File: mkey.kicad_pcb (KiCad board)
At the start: 2 copper layers, 346.1 x 94.5 mm, 168 parts, among them J1 USB_C_REP_2.0, J2 24 pin LCD FPC connector, U1 ESP32-S3-WROOM-1, U2 SY8088

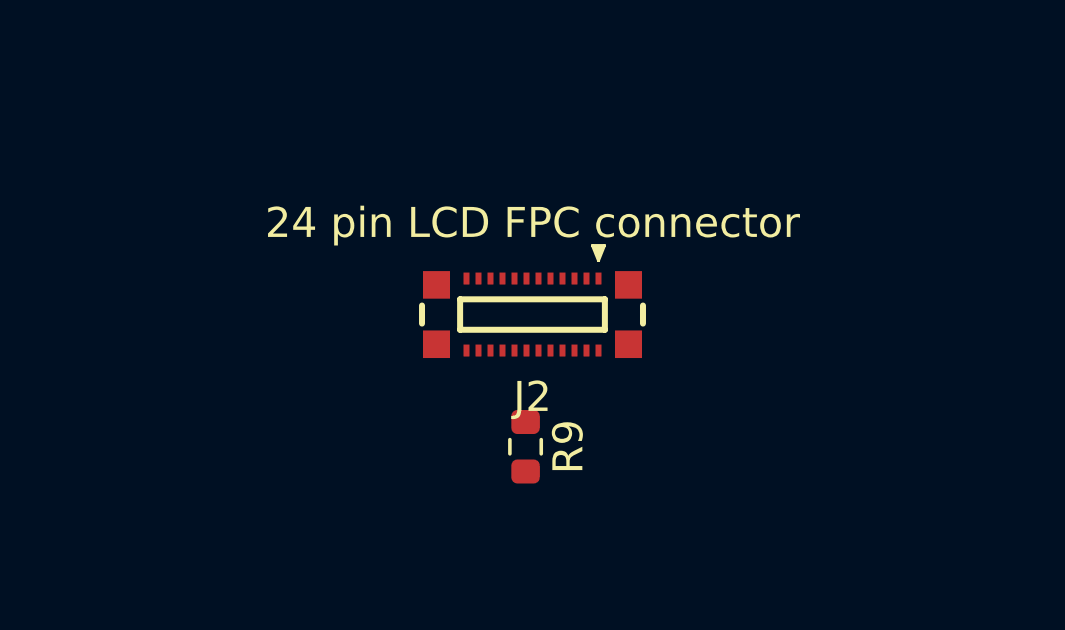
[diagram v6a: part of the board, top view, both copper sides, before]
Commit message: edit connector symbol to layout pins linearly, update pcb
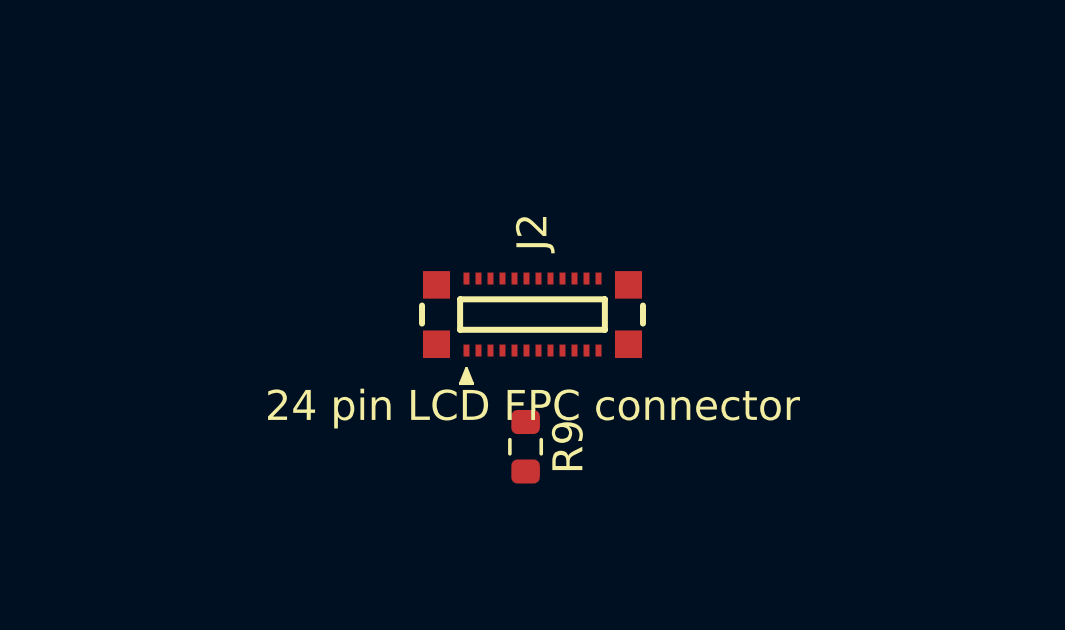
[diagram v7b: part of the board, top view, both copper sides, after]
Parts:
- J2: footprint CONN-SMD_24P-P0.40__X0400FVS-24-LPSN:CONN-SMD_24P-P0.40_X0400FVS-24-LPSN -> CONN-SMD_24P-P0.40_X0400FVS-24-LPSN-LINEAR:CONN-SMD_24P-P0.40_X0400FVS-24-LPSN-LINEAR
- turned J2 to 0 degrees
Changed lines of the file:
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@@
     )
   )
-  (footprint "CONN-SMD_24P-P0.40__X0400FVS-24-LPSN:CONN-SMD_24P-P0.40_X0400FVS-24-LPSN" (layer "F.Cu")
-    (at 358.18122 80.55628 180)
+  (footprint "CONN-SMD_24P-P0.40_X0400FVS-24-LPSN-LINEAR:CONN-SMD_24P-P0.40_X0400FVS-24-LPSN-LINEAR" (layer "F.Cu")
+    (at 358.18122 80.55628)
     (property "Sheetfile" "mkey.kicad_sch")
     (property "Sheetname" "")
     (property "ki_description" "Generic connector, single row, 01x24, script generated")
     (property "ki_keywords" "connector")
-    (fp_text reference "J2" (at 0 -2.75) (layer "F.SilkS")
+    (fp_text reference "J2" (at 0 -2.75 90) (layer "F.SilkS")
         (effects (font (size 1 1) (thickness 0.15)))
     )
@@
         (effects (font (size 1 1) (thickness 0.15)))
     )
-    (fp_text user "${REFERENCE}" (at -2.85557 0.29322 180 unlocked) (layer "Eco2.User")
+    (fp_text user "${REFERENCE}" (at -2.85557 0.29322 unlocked) (layer "Eco2.User")
         (effects (font (size 0.762 0.762) (thickness 0.254)) (justify left bottom))
     )
@@
     (fp_line (start 4 2) (end 4 -2)
       (stroke (width 0.1) (type solid)) (layer "Eco2.User"))
-    (pad "1" smd rect (at -2.20002 1.20002 180) (size 0.2 0.4) (layers "F.Cu" "F.Paste" "F.Mask")
+    (pad "1" smd rect (at 2.19997 -1.2) (size 0.2 0.4) (layers "F.Cu" "F.Paste" "F.Mask")
       (net 118 "LCD_RESET") (pinfunction "Pin_1") (pintype "passive") (thermal_bridge_angle 45))
-    (pad "2" smd rect (at -2.20002 -1.19997 180) (size 0.2 0.4) (layers "F.Cu" "F.Paste" "F.Mask")
+    (pad "2" smd rect (at 1.79997 -1.19997) (size 0.2 0.4) (layers "F.Cu" "F.Paste" "F.Mask")
       (net 7 "GND") (pinfunction "Pin_2") (pintype "passive") (thermal_bridge_angle 45))
-    (pad "3" smd rect (at -1.80002 1.20002 180) (size 0.2 0.4) (layers "F.Cu" "F.Paste" "F.Mask")
+    (pad "3" smd rect (at 1.39997 -1.19997) (size 0.2 0.4) (layers "F.Cu" "F.Paste" "F.Mask")
       (net 119 "TEAR EFFECT") (pinfunction "Pin_3") (pintype "passive") (thermal_bridge_angle 45))
-    (pad "4" smd rect (at -1.80002 -1.19997 180) (size 0.2 0.4) (layers "F.Cu" "F.Paste" "F.Mask")
+    (pad "4" smd rect (at 0.99997 -1.19997) (size 0.2 0.4) (layers "F.Cu" "F.Paste" "F.Mask")
       (net 7 "GND") (pinfunction "Pin_4") (pintype "passive") (thermal_bridge_angle 45))
-    (pad "5" smd rect (at -1.40002 1.20002 180) (size 0.2 0.4) (layers "F.Cu" "F.Paste" "F.Mask")
+    (pad "5" smd rect (at 0.59997 -1.19997) (size 0.2 0.4) (layers "F.Cu" "F.Paste" "F.Mask")
       (net 120 "LCD_CLK") (pinfunction "Pin_5") (pintype "passive") (thermal_bridge_angle 45))
-    (pad "6" smd rect (at -1.40002 -1.19997 180) (size 0.2 0.4) (layers "F.Cu" "F.Paste" "F.Mask")
+    (pad "6" smd rect (at 0.19997 -1.19997) (size 0.2 0.4) (layers "F.Cu" "F.Paste" "F.Mask")
       (net 131 "LCD_SIO1") (pinfunction "Pin_6") (pintype "passive") (thermal_bridge_angle 45))
-    (pad "7" smd rect (at -1.00002 1.20002 180) (size 0.2 0.4) (layers "F.Cu" "F.Paste" "F.Mask")
+    (pad "7" smd rect (at -0.20003 -1.19997) (size 0.2 0.4) (layers "F.Cu" "F.Paste" "F.Mask")
       (net 121 "LCD_SIO0") (pinfunction "Pin_7") (pintype "passive") (thermal_bridge_angle 45))
-    (pad "8" smd rect (at -1.00002 -1.19997 180) (size 0.2 0.4) (layers "F.Cu" "F.Paste" "F.Mask")
+    (pad "8" smd rect (at -0.60002 -1.19997) (size 0.2 0.4) (layers "F.Cu" "F.Paste" "F.Mask")
       (net 7 "GND") (pinfunction "Pin_8") (pintype "passive") (thermal_bridge_angle 45))
-    (pad "9" smd rect (at -0.60002 1.20002 180) (size 0.2 0.4) (layers "F.Cu" "F.Paste" "F.Mask")
+    (pad "9" smd rect (at -1.00002 -1.19997) (size 0.2 0.4) (layers "F.Cu" "F.Paste" "F.Mask")
       (net 116 "unconnected-(J2-Pin_9-Pad9)") (pinfunction "Pin_9") (pintype "passive+no_connect") (thermal_bridge_angle 45))
-    (pad "10" smd rect (at -0.60002 -1.19997 180) (size 0.2 0.4) (layers "F.Cu" "F.Paste" "F.Mask")
+    (pad "10" smd rect (at -1.40002 -1.19997) (size 0.2 0.4) (layers "F.Cu" "F.Paste" "F.Mask")
       (net 117 "unconnected-(J2-Pin_10-Pad10)") (pinfunction "Pin_10") (pintype "passive+no_connect") (thermal_bridge_angle 45))
-    (pad "11" smd rect (at -0.20003 1.20002 180) (size 0.2 0.4) (layers "F.Cu" "F.Paste" "F.Mask")
+    (pad "11" smd rect (at -1.80002 -1.19997) (size 0.2 0.4) (layers "F.Cu" "F.Paste" "F.Mask")
       (net 7 "GND") (pinfunction "Pin_11") (pintype "passive") (thermal_bridge_angle 45))
-    (pad "12" smd rect (at -0.20003 -1.19997 180) (size 0.2 0.4) (layers "F.Cu" "F.Paste" "F.Mask")
+    (pad "12" smd rect (at -2.20002 -1.19997) (size 0.2 0.4) (layers "F.Cu" "F.Paste" "F.Mask")
       (net 7 "GND") (pinfunction "Pin_12") (pintype "passive") (thermal_bridge_angle 45))
-    (pad "13" smd rect (at 0.19997 1.20002 180) (size 0.2 0.4) (layers "F.Cu" "F.Paste" "F.Mask")
+    (pad "13" smd rect (at -2.20002 1.20002) (size 0.2 0.4) (layers "F.Cu" "F.Paste" "F.Mask")
       (net 122 "Net-(J2-Pin_13)") (pinfunction "Pin_13") (pintype "passive") (thermal_bridge_angle 45))
-    (pad "14" smd rect (at 0.19997 -1.19997 180) (size 0.2 0.4) (layers "F.Cu" "F.Paste" "F.Mask")
+    (pad "14" smd rect (at -1.80002 1.20002) (size 0.2 0.4) (layers "F.Cu" "F.Paste" "F.Mask")
       (net 122 "Net-(J2-Pin_13)") (pinfunction "Pin_14") (pintype "passive") (thermal_bridge_angle 45))
-    (pad "15" smd rect (at 0.59997 1.20002 180) (size 0.2 0.4) (layers "F.Cu" "F.Paste" "F.Mask")
+    (pad "15" smd rect (at -1.40002 1.20002) (size 0.2 0.4) (layers "F.Cu" "F.Paste" "F.Mask")
       (net 123 "+3.3V") (pinfunction "Pin_15") (pintype "passive") (thermal_bridge_angle 45))
-    (pad "16" smd rect (at 0.59997 -1.19997 180) (size 0.2 0.4) (layers "F.Cu" "F.Paste" "F.Mask")
+    (pad "16" smd rect (at -1.00002 1.20002) (size 0.2 0.4) (layers "F.Cu" "F.Paste" "F.Mask")
       (net 123 "+3.3V") (pinfunction "Pin_16") (pintype "passive") (thermal_bridge_angle 45))
-    (pad "17" smd rect (at 0.99997 1.20002 180) (size 0.2 0.4) (layers "F.Cu" "F.Paste" "F.Mask")
+    (pad "17" smd rect (at -0.60002 1.20002) (size 0.2 0.4) (layers "F.Cu" "F.Paste" "F.Mask")
       (net 124 "TP_INT") (pinfunction "Pin_17") (pintype "passive") (thermal_bridge_angle 45))
-    (pad "18" smd rect (at 0.99997 -1.19997 180) (size 0.2 0.4) (layers "F.Cu" "F.Paste" "F.Mask")
+    (pad "18" smd rect (at -0.20003 1.20002) (size 0.2 0.4) (layers "F.Cu" "F.Paste" "F.Mask")
       (net 130 "TP_RST") (pinfunction "Pin_18") (pintype "passive") (thermal_bridge_angle 45))
-    (pad "19" smd rect (at 1.39997 1.20002 180) (size 0.2 0.4) (layers "F.Cu" "F.Paste" "F.Mask")
+    (pad "19" smd rect (at 0.19997 1.20002) (size 0.2 0.4) (layers "F.Cu" "F.Paste" "F.Mask")
       (net 125 "TP_SDA") (pinfunction "Pin_19") (pintype "passive") (thermal_bridge_angle 45))
-    (pad "20" smd rect (at 1.39997 -1.19997 180) (size 0.2 0.4) (layers "F.Cu" "F.Paste" "F.Mask")
+    (pad "20" smd rect (at 0.59997 1.20002) (size 0.2 0.4) (layers "F.Cu" "F.Paste" "F.Mask")
       (net 129 "TP_SCL") (pinfunction "Pin_20") (pintype "passive") (thermal_bridge_angle 45))
-    (pad "21" smd rect (at 1.79997 1.20002 180) (size 0.2 0.4) (layers "F.Cu" "F.Paste" "F.Mask")
+    (pad "21" smd rect (at 0.99997 1.20002) (size 0.2 0.4) (layers "F.Cu" "F.Paste" "F.Mask")
       (net 7 "GND") (pinfunction "Pin_21") (pintype "passive") (thermal_bridge_angle 45))
-    (pad "22" smd rect (at 1.79997 -1.19997 180) (size 0.2 0.4) (layers "F.Cu" "F.Paste" "F.Mask")
+    (pad "22" smd rect (at 1.39997 1.20002) (size 0.2 0.4) (layers "F.Cu" "F.Paste" "F.Mask")
       (net 128 "LCD_SIO3") (pinfunction "Pin_22") (pintype "passive") (thermal_bridge_angle 45))
-    (pad "23" smd rect (at 2.19997 1.20002 180) (size 0.2 0.4) (layers "F.Cu" "F.Paste" "F.Mask")
+    (pad "23" smd rect (at 1.79997 1.20002) (size 0.2 0.4) (layers "F.Cu" "F.Paste" "F.Mask")
       (net 126 "LCD_SIO4") (pinfunction "Pin_23") (pintype "passive") (thermal_bridge_angle 45))
-    (pad "24" smd rect (at 2.19997 -1.2 180) (size 0.2 0.4) (layers "F.Cu" "F.Paste" "F.Mask")
+    (pad "24" smd rect (at 2.19997 1.20002) (size 0.2 0.4) (layers "F.Cu" "F.Paste" "F.Mask")
       (net 127 "LCD_D{slash}C") (pinfunction "Pin_24") (pintype "passive") (thermal_bridge_angle 45))
-    (pad "25" smd rect (at 3.20002 -0.98997 180) (size 0.9 0.91999) (layers "F.Cu" "F.Paste" "F.Mask")
+    (pad "25" smd rect (at 3.20002 -0.98997) (size 0.9 0.91999) (layers "F.Cu" "F.Paste" "F.Mask")
       (thermal_bridge_angle 45))
-    (pad "26" smd rect (at 3.20002 0.99002 180) (size 0.9 0.91999) (layers "F.Cu" "F.Paste" "F.Mask")
+    (pad "26" smd rect (at 3.20002 0.99002) (size 0.9 0.91999) (layers "F.Cu" "F.Paste" "F.Mask")
       (thermal_bridge_angle 45))
-    (pad "27" smd rect (at -3.19997 0.99002 180) (size 0.9 0.91999) (layers "F.Cu" "F.Paste" "F.Mask")
+    (pad "27" smd rect (at -3.19997 0.99002) (size 0.9 0.91999) (layers "F.Cu" "F.Paste" "F.Mask")
       (thermal_bridge_angle 45))
-    (pad "28" smd rect (at -3.19997 -0.98997 180) (size 0.9 0.91999) (layers "F.Cu" "F.Paste" "F.Mask")
+    (pad "28" smd rect (at -3.19997 -0.98997) (size 0.9 0.91999) (layers "F.Cu" "F.Paste" "F.Mask")
       (thermal_bridge_angle 45))
   )

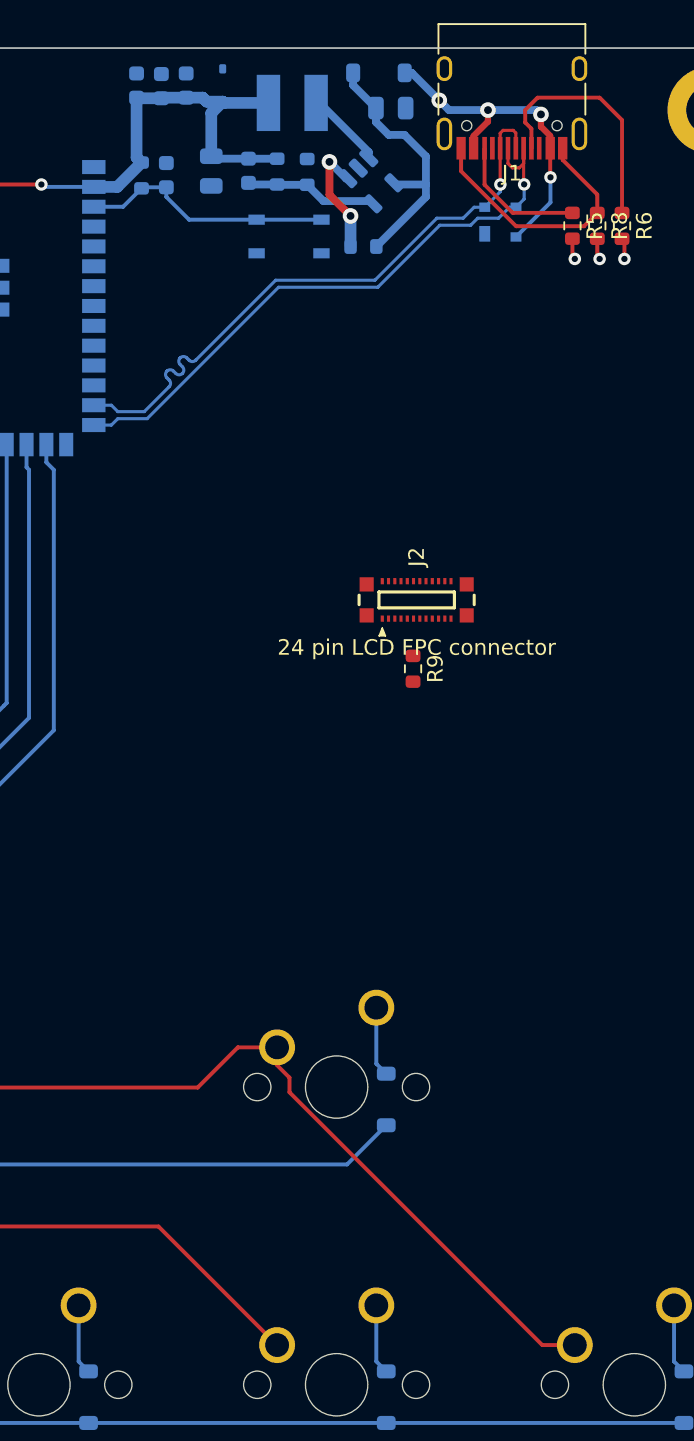
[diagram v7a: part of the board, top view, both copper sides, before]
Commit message: Added display silk and connector. Began routing of connector. Dropped support for external jtag
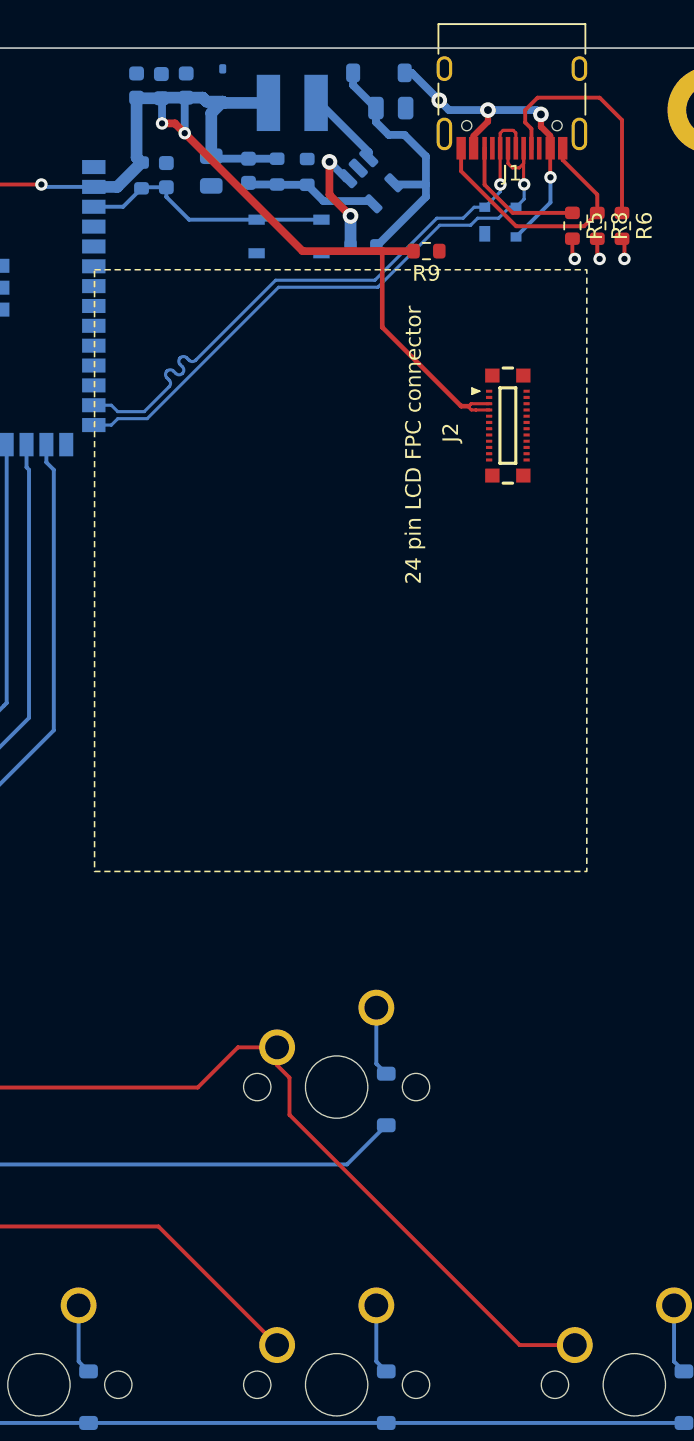
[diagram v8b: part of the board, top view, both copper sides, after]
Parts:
- J2: footprint CONN-SMD_24P-P0.40_X0400FVS-24-LPSN-LINEAR:CONN-SMD_24P-P0.40_X0400FVS-24-LPSN-LINEAR -> 24P_LCD_CONN:CONN-SMD_24P-P0.40_X0400FVS-24-LPSN-LINEAR
- moved J2 29.5 mm to (337.6, 59.4)
- moved R9 26.7 mm to (358.8, 58.2), turned to 180 degrees
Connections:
- C3 pad 1: CHIP_POWER -> +3V3
- C4 pad 1: CHIP_POWER -> +3V3
- C5 pad 1: CHIP_POWER -> +3V3
- C6 pad 1: CHIP_POWER -> +3V3
- C7 pad 1: CHIP_POWER -> +3V3
- D68 pad 2: CHIP_POWER -> +3V3
- J2 pad 15: +3.3V -> +3V3
- J2 pad 16: +3.3V -> +3V3
- L1 pad 2: CHIP_POWER -> +3V3
- R1 pad 1: CHIP_POWER -> +3V3
- R3 pad 1: CHIP_POWER -> +3V3
- R7 pad 1: CHIP_POWER -> +3V3
- R9 pad 2: +3.3V -> +3V3
- U1 pad 10: unconnected-(U1-GPIO17/U1TXD/ADC2_CH6-Pad10) -> LCD_SIO3
- U1 pad 11: unconnected-(U1-GPIO18/U1RXD/ADC2_CH7/CLK_OUT3-Pad11) -> LCD_SIO4
- U1 pad 12: unconnected-(U1-GPIO8/TOUCH8/ADC1_CH7/SUBSPICS1-Pad12) -> TEAR EFFECT
- U1 pad 15: unconnected-(U1-GPIO3/TOUCH3/ADC1_CH2-Pad15) -> LCD_RESET
- U1 pad 2: CHIP_POWER -> +3V3
- U1 pad 32: unconnected-(U1-MTCK/GPIO39/CLK_OUT3/SUBSPICS1-Pad32) -> TP_INT
- U1 pad 33: unconnected-(U1-MTDO/GPIO40/CLK_OUT2-Pad33) -> TP_RST
- U1 pad 34: unconnected-(U1-MTDI/GPIO41/CLK_OUT1-Pad34) -> TP_SDA
- U1 pad 35: unconnected-(U1-MTMS/GPIO42-Pad35) -> TP_SCL
- U1 pad 5: unconnected-(U1-GPIO5/TOUCH5/ADC1_CH4-Pad5) -> LCD_D/C
- U1 pad 7: unconnected-(U1-GPIO7/TOUCH7/ADC1_CH6-Pad7) -> LCD_CLK
- U1 pad 8: unconnected-(U1-GPIO15/U0RTS/ADC2_CH4/XTAL_32K_P-Pad8) -> LCD_SIO0
- U1 pad 9: unconnected-(U1-GPIO16/U0CTS/ADC2_CH5/XTAL_32K_N-Pad9) -> LCD_SIO1
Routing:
- net +3V3: track 0.00 -> 100.9 mm, vias 0 -> 4
- net CHIP_POWER: track 62.2 -> 0.00 mm, vias 2 -> 0
- net COL13: track 170.8 -> 171.6 mm
